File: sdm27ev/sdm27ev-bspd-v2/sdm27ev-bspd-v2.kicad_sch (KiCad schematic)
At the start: 4 parts, among them J1 776280-1, J2 776280-1, J3 Conn_01x01_Socket, J4 Conn_01x01_Socket

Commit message: Started working on V2 BSPD
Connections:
- net BRAKE SENSOR: now also J1.4 (Pin_4); no longer J1.8 (Pin_8)
- net GND: now also J1.8 (Pin_8), J2.3 (Pin_3); no longer J1.4 (Pin_4), J2.5 (Pin_5)
- net +5V_BMS: now reaches J2.6 (Pin_6)
- no-connect marks 0 -> 1
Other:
- added sheet Current Sensor Sub-Board (Current Sensor.kicad_sch)
- note added: "Batt. Nominal: 330V Trip Power: 5kW Trip Current: P = IV ⇒ I = P/V I = 5000W/330V = 15.15A Current per loop = I / n_{loops} I_{test} = 15.15A/15 ≈ 1A"
- note added: "External Wireing Harness"

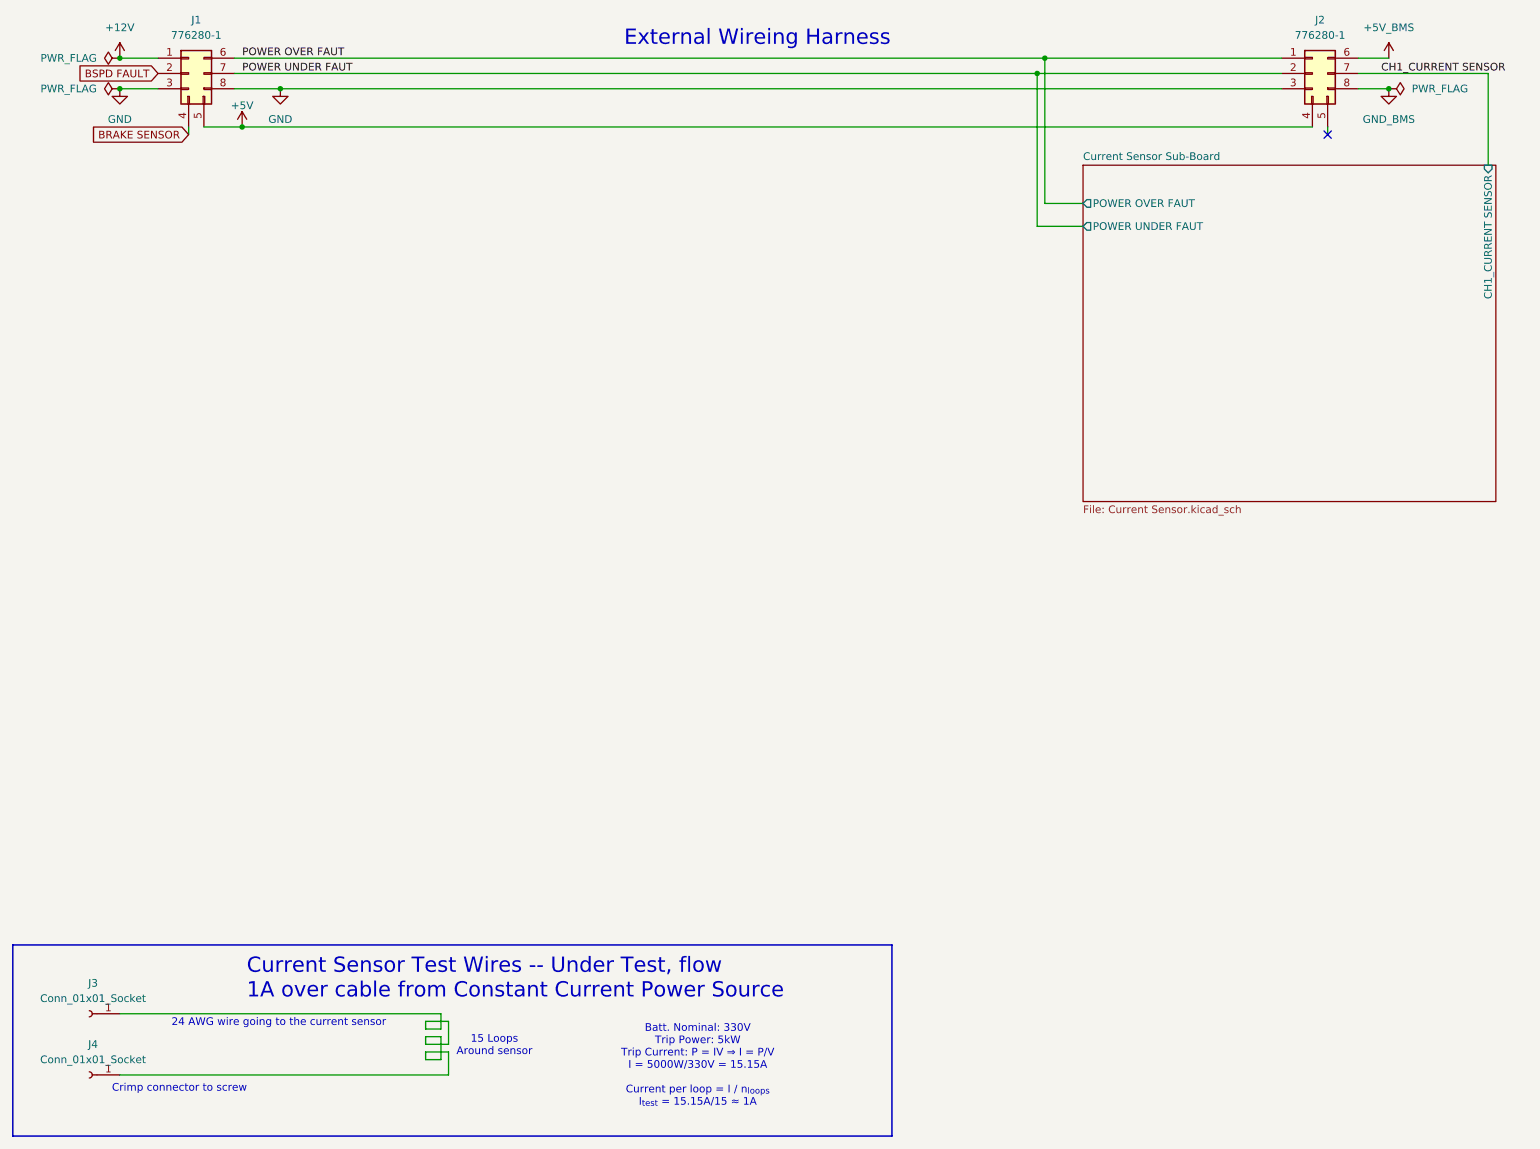
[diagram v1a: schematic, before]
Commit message: Tentitive Schematic for BSPD
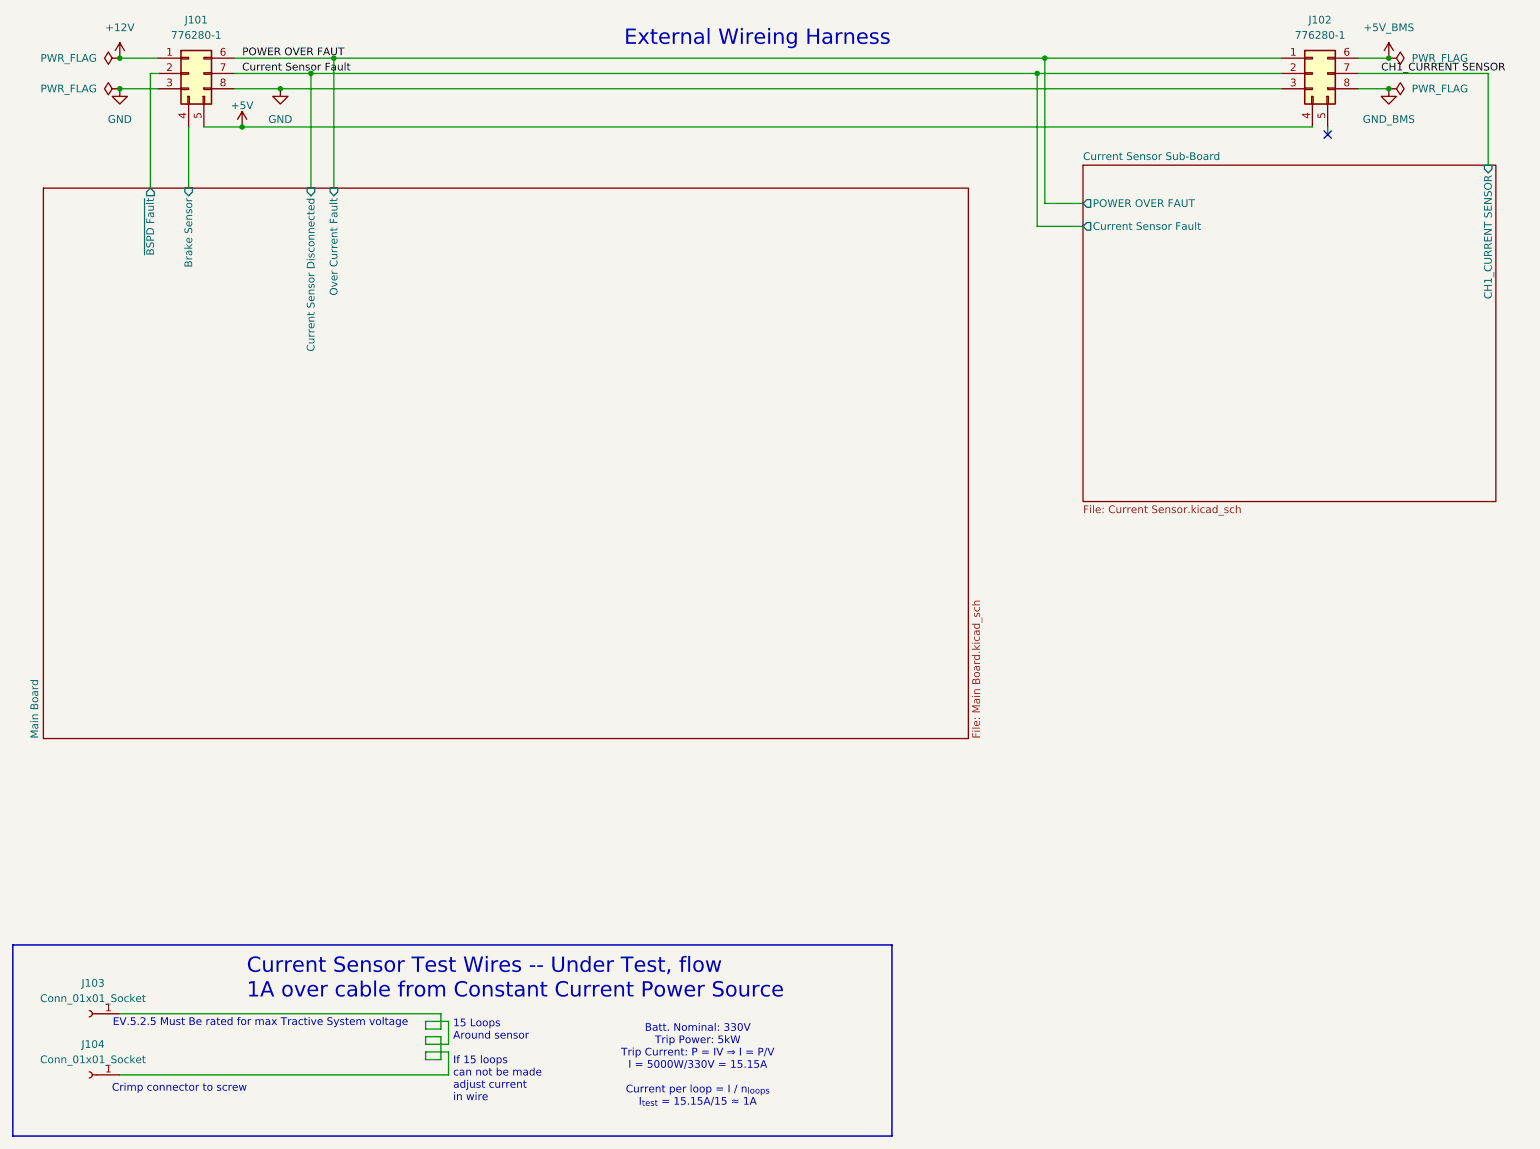
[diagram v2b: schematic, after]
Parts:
- renumbered J1 to J101, J2 to J102, J3 to J103, J4 to J104
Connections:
- net BRAKE SENSOR renamed Main Board/Brake Sensor
- net BSPD FAULT renamed Main Board/~{BSPD Fault}
- net POWER UNDER FAUT renamed Current Sensor Fault
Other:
- added sheet Main Board (Main Board.kicad_sch)
- sheet Current Sensor Sub-Board ports: added Current Sensor Fault; removed POWER UNDER FAUT
- note added: "15 Loops Around sensor If 15 loops can not be made adjust current in wire"
- note added: "EV.5.2.5 Must Be rated for max Tractive System voltage"
- note removed: "15 Loops Around sensor"
- note removed: "24 AWG wire going to the current sensor"

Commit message: small referance changes
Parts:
- J101, J102: footprint 776280-1 -> SDM_MiscFootprint:776280-1
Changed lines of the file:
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@@
 		(exclude_from_sim no)
 		(in_bom yes)
-		(on_board yes)
+		(on_board no)
 		(in_pos_files yes)
 		(dnp no)
@@
 			)
 		)
-		(property "Footprint" "776280-1"
+		(property "Footprint" "SDM_MiscFootprint:776280-1"
 			(at 53.34 119.05 0)
 			(hide yes)
@@
 		(exclude_from_sim no)
 		(in_bom yes)
-		(on_board yes)
+		(on_board no)
 		(in_pos_files yes)
 		(dnp no)
@@
 			)
 		)
-		(property "Footprint" "776280-1"
+		(property "Footprint" "SDM_MiscFootprint:776280-1"
 			(at 240.03 119.05 0)
 			(hide yes)

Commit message: Updated BSPD Schematic
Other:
- note added: "Link to Falstad Simulation"
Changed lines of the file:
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@@
+		)
+	)
+	(rectangle
+		(start 191.77 110.49)
+		(end 245.11 116.84)
+		(stroke
+			(width 0)
+			(type default)
+		)
+		(fill
+			(type none)
 		)
 	)
@@
 		)
 	)
+	(text "Link to Falstad Simulation"
+		(exclude_from_sim no)
+		(at 218.186 113.792 0)
+		(effects
+			(font
+				(size 2.54 2.54)
+			)
+			(href "https://links.dylan-shah.com/sdm-bspd-falstad")
+		)
+	)
